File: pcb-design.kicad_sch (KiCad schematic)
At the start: 7 parts, among them J2 SM06B-SRSS-TBLFSN, U2 OS102011MA1QS1, U4 MOUDLE-SEEEDUINO-XIAO-ESP32C3

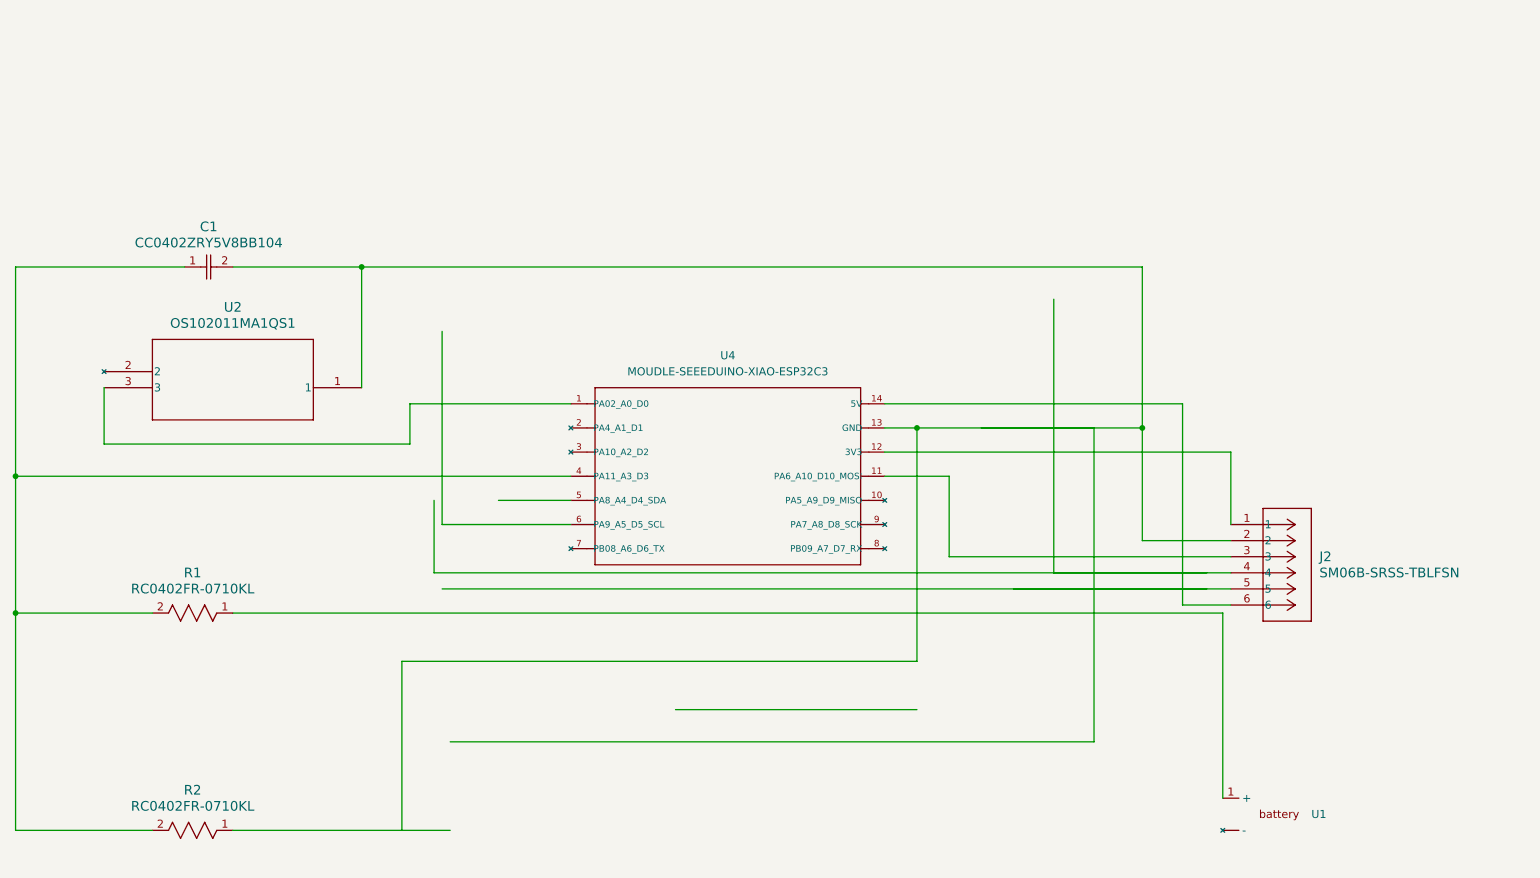
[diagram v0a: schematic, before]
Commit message: 3.3v new temp
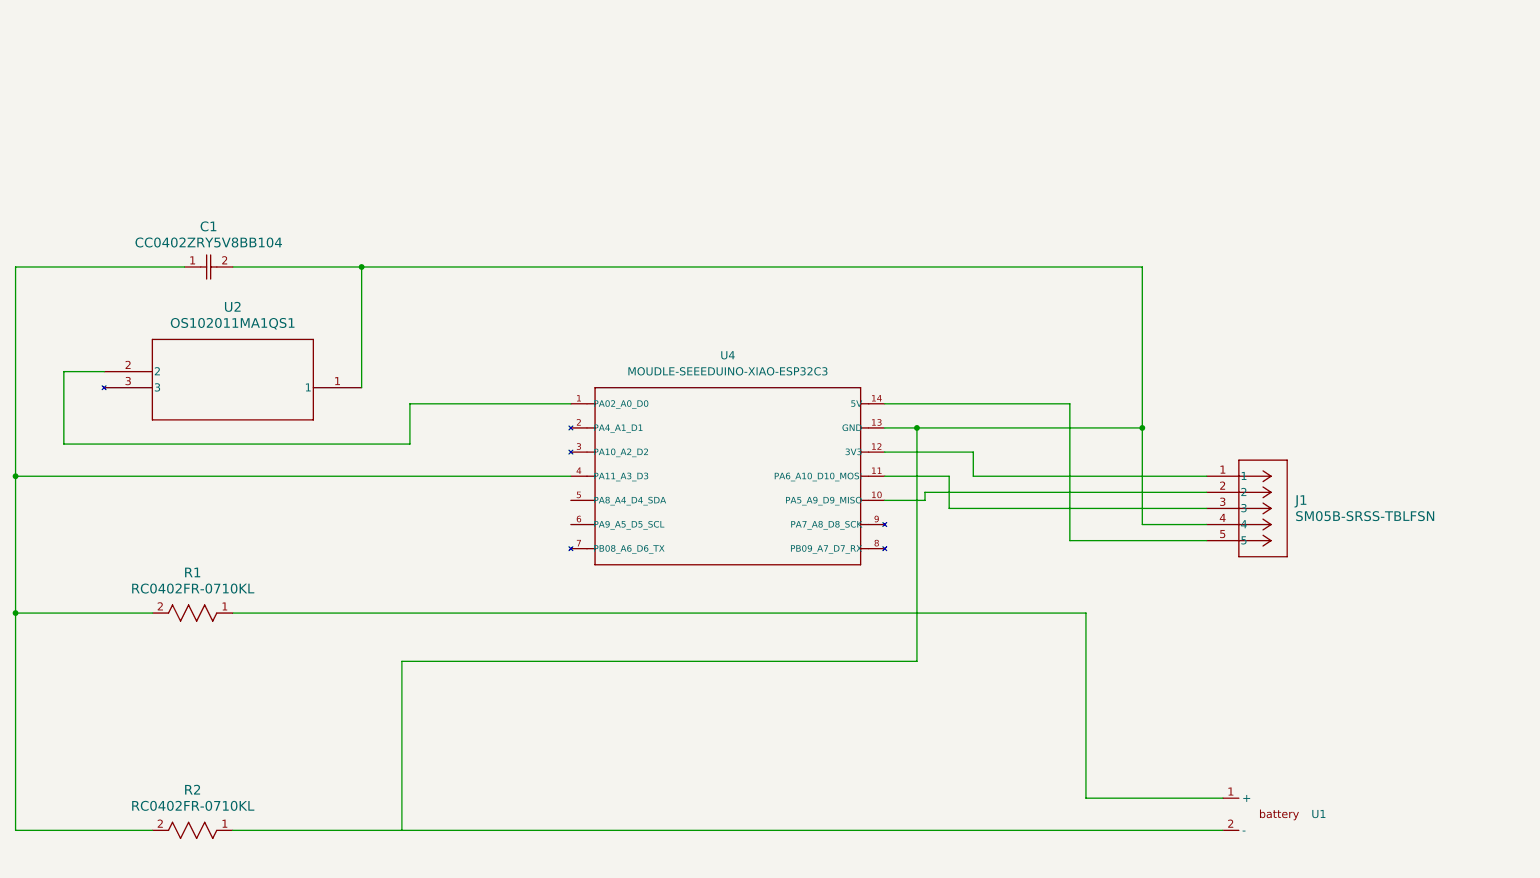
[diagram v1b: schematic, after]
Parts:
- removed J2: SM06B-SRSS-TBLFSN, CONN_SM06B-SRSS-TB_JST, symbol SM06B-SRSS-TB:SM06B-SRSS-TBLFSN
- added J1: SM05B-SRSS-TBLFSN, CONN5_SM05B-SRSS_JST, symbol 2023-11-23_21-58-41:SM05B-SRSS-TBLFSN
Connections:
- net at U4.1 (PA02_A0_D0): now also U2.2; no longer U2.3
- net at U4.10 (PA5_A9_D9_MISO): now also J1.2
- net at U4.11 (PA6_A10_D10_MOSI): now also J1.3
- net at U4.12 (3V3): now also J1.1
- net at C1.2, U2.1, U4.13 (GND): now also J1.4
- net at U4.14 (5V): now also J1.5
- net at R2.1: now also U1.2 (-)

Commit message: header for 4-new pcb...
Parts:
- removed J1: SM05B-SRSS-TBLFSN, CONN5_SM05B-SRSS_JST, symbol 2023-11-23_21-58-41:SM05B-SRSS-TBLFSN
- added J2: SM04B-SRSS-TBLFSN, Connector_JST:JST_SH_SM04B-SRSS-TB_1x04-1MP_P1.00mm_Horizontal, symbol 2024-04-08_19-38-15:SM04B-SRSS-TBLFSN
- added R3, R4: RC0402FR-0710KL, RC0402N_YAG, symbol 2023-11-23_19-25-58:RC0402FR-0710KL
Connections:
- net at U4.10 (PA5_A9_D9_MISO): now also R3.2
- net at U4.11 (PA6_A10_D10_MOSI): now also J2.2
- net at C1.2, U2.1, U4.13 (GND): now also J2.3, R4.1
- net at U4.14 (5V): now also J2.4
- new net: J2.1, R3.1, R4.2

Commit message: met transistor
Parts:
- added Q1: AOSS32338C, Package_TO_SOT_SMD:TSOT-23, symbol 2024-04-09_19-22-22:AOSS32338C
- added R5: RC0402FR-0710KL, RC0402N_YAG, symbol 2023-11-23_19-25-58:RC0402FR-0710KL
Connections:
- net at U4.1 (PA02_A0_D0): now also C1.1, R1.2, R2.2; no longer U2.2
- net esp-3.3: now reaches U4.12 (3V3)
- net esp-3.3: now also U2.3, Q1.2 (S)
- net gnd: now reaches C1.2, J2.3, R4.1, U2.1, U4.13 (GND)
- net gnd: now also R2.1, U1.2 (-)
- net at U4.14 (5V): no longer J2.4
- net D1: now reaches U4.2 (PA4_A1_D1)
- net D1: now also U2.2, R5.1
- net B+: now reaches R1.1, U1.1 (+)
- new net: Q1.1 (G), R5.2
- new net header-3.3: J2.4, Q1.3 (D)
- now unconnected: U4.4 (PA11_A3_D3)
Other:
- moved on the sheet: R1, R3, R4, U1

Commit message: v.4.0.6
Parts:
- removed Q1: AOSS32338C, Package_TO_SOT_SMD:TSOT-23, symbol 2024-04-09_19-22-22:AOSS32338C
- removed R3, R4, R5: RC0402FR-0710KL, RC0402N_YAG, symbol 2023-11-23_19-25-58:RC0402FR-0710KL
- added D2: SK6812, LED_SMD:LED_WS2812B-Mini_PLCC4_3.5x3.5mm, symbol LED:SK6812
- added Q2: NPN, Package_TO_SOT_SMD:SOT-23-3, symbol Simulation_SPICE:NPN
- added R3: RC0402JR-07560RL, ul_RC0402FR-0710KL:RC0402N_YAG, symbol 2024-04-11_18-56-32:RC0402JR-07560RL
- added U3: TSIC206-TO92, Connector_PinHeader_1.00mm:PinHeader_1x03_P1.00mm_Vertical, symbol Sensor_Temperature:TSIC206-TO92
- U4: footprint MOUDLE14P-SMD-2.54-21X17.8MM -> xiao ESP32C3_PCBa:MOUDLE14P-SMD-2.54-21X17.8MM
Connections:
- net header-3.3 is gone; now on net esp-3.3: J2.4
- net esp-3.3: now also U2.1; no longer U2.3
- net D8: now reaches J2.1
- net D8: now also U4.9 (PA7_A8_D8_SCK)
- net at C1.1, R1.2, R2.2: now also U4.3 (PA10_A2_D2); no longer U4.1 (PA02_A0_D0)
- net D10: now reaches J2.2, U4.11 (PA6_A10_D10_MOSI)
- net D1: no longer names the net of U4.2 (PA4_A1_D1)
- net D1: no longer U2.2
- net gnd renamed esp-gnd
- net esp-gnd: now also U2.3, Q2.3 (E); no longer J2.3, U1.2 (-), U2.1
- new net: Q2.2 (B), R3.2
- new net G: J2.3, Q2.1 (C)
- new net SW-OUT: R3.1, U2.2, U4.1 (PA02_A0_D0)

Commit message: v4.0.8
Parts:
- removed Q2: NPN, Package_TO_SOT_SMD:SOT-23-3, symbol Simulation_SPICE:NPN
- added J1: SM04B-SRSS-TBLFSN, Breakout_Connector:Breakout_conn, symbol 2024-04-08_19-38-15:SM04B-SRSS-TBLFSN
- added U5: ~, TestPoint:TestPoint_2Pads_Pitch2.54mm_Drill0.8mm, symbol my_custom_symbol_library:pcb-battery-connector
- U3: footprint Connector_PinHeader_1.00mm:PinHeader_1x03_P1.00mm_Vertical -> Connector_PinHeader_1.5mm:PinHeader_1x03_P1.5mm_Vertical
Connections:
- net B+: now also U5.1 (+)
- net SW-OUT: now also J2.4, R3.2; no longer R3.1, U4.1 (PA02_A0_D0)
- net esp-3.3: no longer J2.4
- net B-: now reaches U1.2 (-)
- net B-: now also U5.2 (-)
- net 3.3v: now reaches U3.1 (V+)
- net 3.3v: now also D2.3 (VDD), J1.4
- net Temp: now reaches U3.2 (Signal)
- net Temp: now also J1.1
- net GND: now reaches U3.3 (GND)
- net GND: now also D2.1 (VSS), J1.3
- net Licht: now reaches D2.2 (DIN)
- net Licht: now also J1.2
- new net D0: R3.1, U4.1 (PA02_A0_D0)
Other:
- moved on the sheet: D2, U3

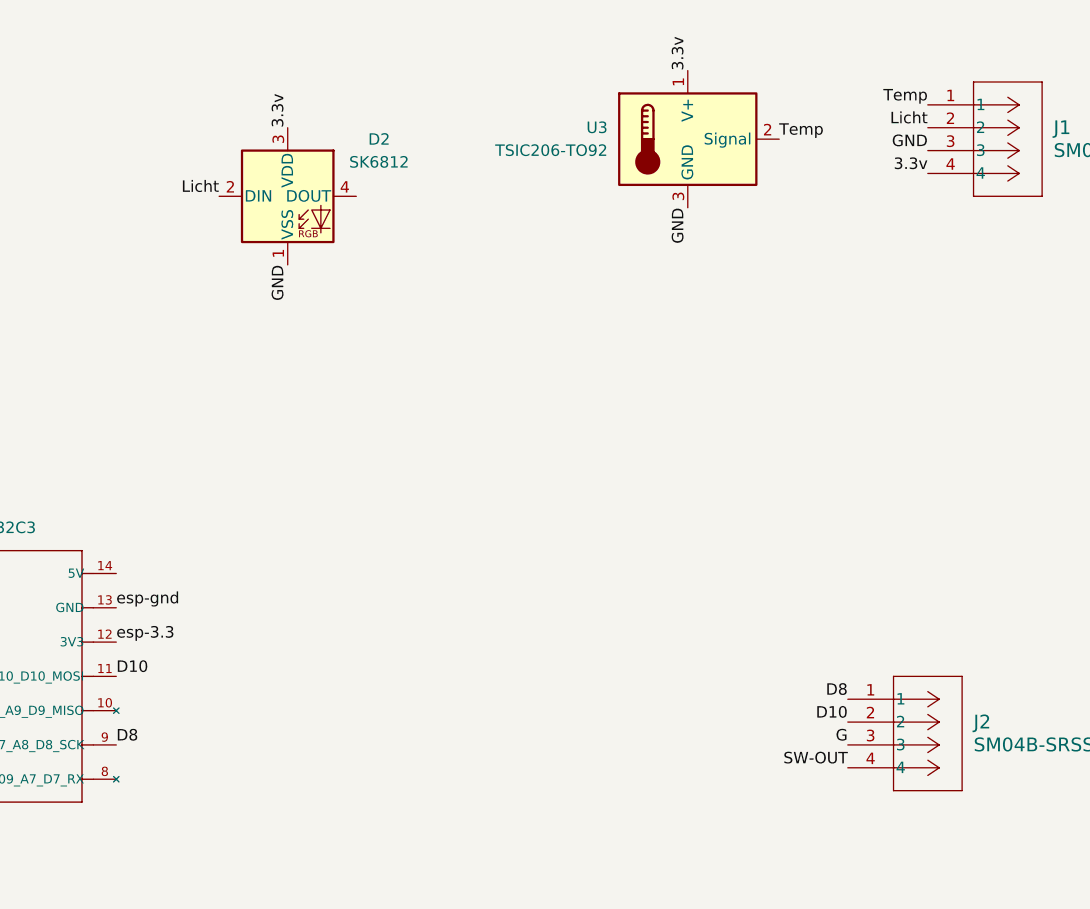
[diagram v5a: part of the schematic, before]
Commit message: plus ground-header+tempsensor en light differently arranged
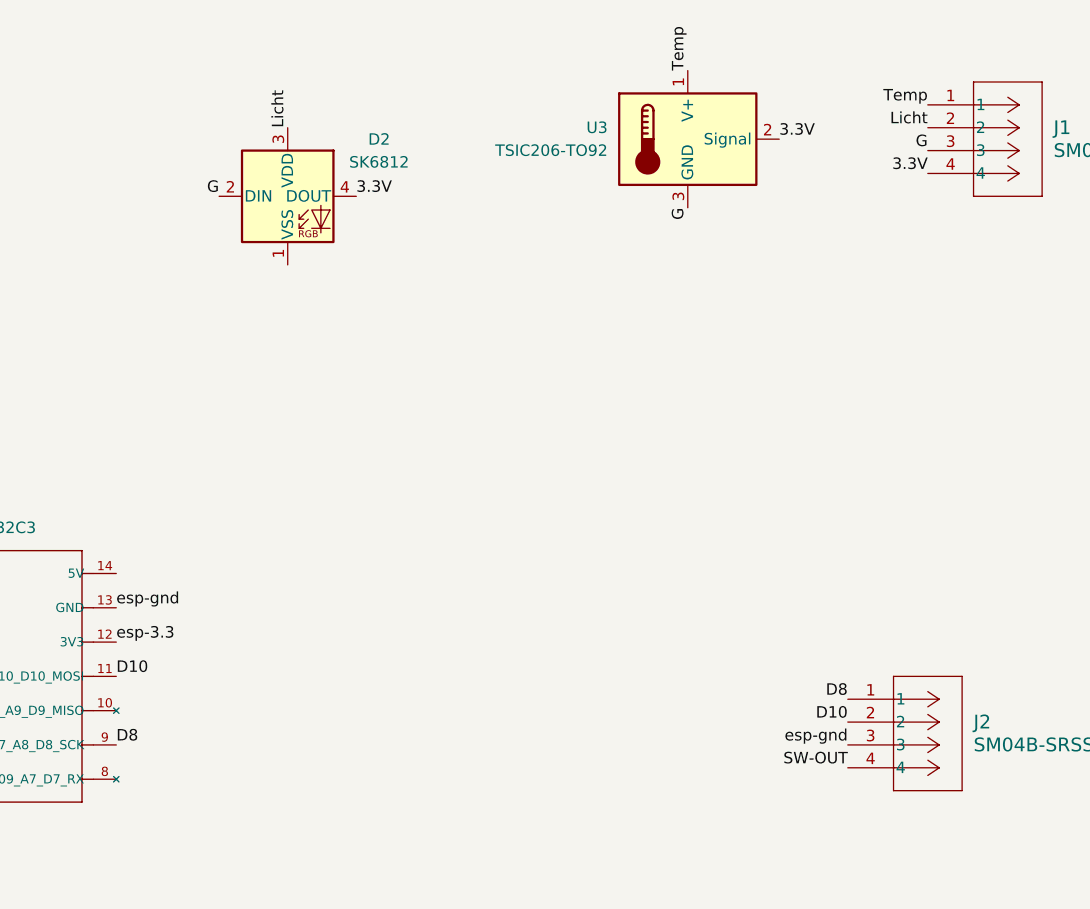
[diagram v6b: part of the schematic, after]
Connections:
- net G: now also D2.2 (DIN), J1.3, U3.3 (GND); no longer J2.3
- net Licht: now also D2.3 (VDD); no longer D2.2 (DIN)
- net Temp: now also U3.1 (V+); no longer U3.2 (Signal)
- net esp-gnd: now also J2.3
- net 3.3V: now reaches D2.4 (DOUT)
- net 3.3V: now also J1.4, U3.2 (Signal)
- removed net 3.3v: D2.3 (VDD), J1.4, U3.1 (V+)
- removed net GND: D2.1 (VSS), J1.3, U3.3 (GND)
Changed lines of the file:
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@@
+		)
+	)
+	(label "Licht"
+		(at 173.99 25.4 90)
+		(fields_autoplaced yes)
+		(effects
+			(font
+				(size 1.27 1.27)
+			)
+			(justify left bottom)
 		)
 	)
@@
 		)
 	)
-	(label "3.3v"
-		(at 245.11 30.48 180)
-		(fields_autoplaced yes)
-		(effects
-			(font
-				(size 1.27 1.27)
-			)
-			(justify right bottom)
-		)
-	)
-	(label "Temp"
-		(at 228.6 26.67 0)
-		(fields_autoplaced yes)
-		(effects
-			(font
-				(size 1.27 1.27)
-			)
-			(justify left bottom)
-		)
-	)
 	(label "esp-gnd"
 		(at 82.55 53.34 0)
@@
 		)
 	)
+	(label "G"
+		(at 245.11 27.94 180)
+		(fields_autoplaced yes)
+		(effects
+			(font
+				(size 1.27 1.27)
+			)
+			(justify right bottom)
+		)
+	)
 	(label "D10"
 		(at 236.22 91.44 180)
@@
 		)
 	)
+	(label "3.3V"
+		(at 228.6 26.67 0)
+		(fields_autoplaced yes)
+		(effects
+			(font
+				(size 1.27 1.27)
+			)
+			(justify left bottom)
+		)
+	)
+	(label "Temp"
+		(at 218.44 19.05 90)
+		(fields_autoplaced yes)
+		(effects
+			(font
+				(size 1.27 1.27)
+			)
+			(justify left bottom)
+		)
+	)
 	(label "esp-gnd"
 		(at 71.12 30.48 180)
@@
 		)
 	)
-	(label "Licht"
-		(at 166.37 33.02 180)
-		(fields_autoplaced yes)
-		(effects
-			(font
-				(size 1.27 1.27)
-			)
-			(justify right bottom)
-		)
-	)
 	(label "B+"
 		(at 226.06 124.46 180)
@@
 		)
 	)
-	(label "GND"
-		(at 173.99 40.64 270)
+	(label "G"
+		(at 166.37 33.02 180)
 		(fields_autoplaced yes)
 		(effects
@@
 		)
 	)
+	(label "3.3V"
+		(at 245.11 30.48 180)
+		(fields_autoplaced yes)
+		(effects
+			(font
+				(size 1.27 1.27)
+			)
+			(justify right bottom)
+		)
+	)
 	(label "SW-OUT"
 		(at 236.22 96.52 180)
@@
 		)
 	)
-	(label "G"
-		(at 236.22 93.98 180)
-		(fields_autoplaced yes)
-		(effects
-			(font
-				(size 1.27 1.27)
-			)
-			(justify right bottom)
-		)
-	)
 	(label "esp-gnd"
 		(at 95.25 142.24 0)
@@
 		)
 	)
-	(label "GND"
+	(label "G"
 		(at 218.44 34.29 270)
 		(fields_autoplaced yes)
@@
 			)
 			(justify right bottom)
-		)
-	)
-	(label "GND"
-		(at 245.11 27.94 180)
-		(fields_autoplaced yes)
-		(effects
-			(font
-				(size 1.27 1.27)
-			)
-			(justify right bottom)
-		)
-	)
-	(label "3.3v"
-		(at 173.99 25.4 90)
-		(fields_autoplaced yes)
-		(effects
-			(font
-				(size 1.27 1.27)
-			)
-			(justify left bottom)
 		)
 	)
@@
 		)
 	)
-	(label "3.3v"
-		(at 218.44 19.05 90)
-		(fields_autoplaced yes)
-		(effects
-			(font
-				(size 1.27 1.27)
-			)
-			(justify left bottom)
+	(label "esp-gnd"
+		(at 236.22 93.98 180)
+		(fields_autoplaced yes)
+		(effects
+			(font
+				(size 1.27 1.27)
+			)
+			(justify right bottom)
 		)
 	)
@@
 		(fields_autoplaced yes)
 		(effects
+			(font
+				(size 1.27 1.27)
+			)
+			(justify left bottom)
+		)
+	)
+	(label "3.3V"
+		(at 181.61 33.02 0)
+		(fields_autoplaced yes)
+		(effects
